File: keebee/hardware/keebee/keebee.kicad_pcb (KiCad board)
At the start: 2 copper layers, 275 x 103 mm, 153 parts, among them J1 USB_B_Micro, J2 Conn_ARM_JTAG_SWD_10, SW1 SW_SPST, SW10 SW_SPST, SW11 SW_SPST, SW12 SW_SPST, SW13 SW_SPST, SW14 SW_SPST, SW15 SW_SPST, SW16 SW_SPST, SW17 SW_SPST, SW18 SW_SPST, SW19 SW_SPST, SW2 SW_SPST, SW20 SW_SPST, SW21 SW_SPST, SW22 SW_SPST, SW23 SW_SPST, SW24 SW_SPST, SW25 SW_SPST, SW26 SW_SPST, SW27 SW_SPST, SW28 SW_SPST, SW29 SW_SPST, SW3 SW_SPST, SW30 SW_SPST, SW31 SW_SPST, SW32 SW_SPST, SW33 SW_SPST, SW34 SW_SPST, SW35 SW_SPST, SW36 SW_SPST, SW37 SW_SPST, SW38 SW_SPST, SW39 SW_SPST, SW4 SW_SPST, SW41 SW_SPST, SW42 SW_SPST, SW43 SW_SPST, SW44 SW_SPST, SW45 SW_SPST, SW46 SW_SPST, SW47 SW_SPST, SW48 SW_SPST, SW49 SW_SPST, SW5 SW_SPST, SW50 SW_SPST, SW51 SW_SPST, SW52 SW_SPST, SW53 SW_SPST, SW54 SW_SPST, SW55 SW_SPST, SW56 SW_SPST, SW57 SW_SPST, SW58 SW_SPST, SW59 SW_SPST, SW6 SW_SPST, SW60 SW_SPST, SW61 SW_SPST, SW62 SW_SPST, SW63 SW_SPST, SW64 SW_SPST, SW65 SW_SPST, SW66 SW_SPST, SW67 SW_SPST, SW68 SW_SPST, SW69 SW_SPST, SW7 SW_SPST, SW70 SW_SPST, SW8 SW_SPST, SW9 SW_SPST, U1 LM1117-3.3, U2 STM32F042K6Tx

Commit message: Finish routing all nets.
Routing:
- net +3V3: track 5.67 -> 415.1 mm, vias 0 -> 7
- net Net-(J1-Pad3): track 0.00 -> 187.2 mm, vias 0 -> 3
- net Net-(J1-Pad2): track 0.00 -> 180.5 mm, vias 0 -> 3
- net GND: track 0.00 -> 79.7 mm, vias 0 -> 15
- net Net-(R1-Pad1): track 0.00 -> 78.6 mm, vias 0 -> 7
- net /SWCLK: track 0.00 -> 56.3 mm
- net Net-(SW40-Pad2): track 0.00 -> 55.4 mm, vias 0 -> 4
- net /SWDIO: track 0.00 -> 54.5 mm, vias 0 -> 4
- net Net-(J1-Pad6): track 0.00 -> 25.0 mm, vias 0 -> 2
- net /COL8: track 98.9 -> 119.6 mm, vias 7 -> 11
- net /COL4: track 114.1 -> 134.6 mm, vias 7 -> 9
- net /COL1: track 180.2 -> 199.8 mm, vias 7 -> 9
- net /VBUS: track 0.00 -> 13.7 mm, vias 0 -> 1
- net Net-(D6-Pad2): track 0.00 -> 8.85 mm
- net Net-(D41-Pad2): track 0.00 -> 3.05 mm
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- added copper zone on B.Cu, net GND
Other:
- net class 3.3v added: clearance 0.2, trace_width 0.5, via_dia 0.8, via_drill 0.4

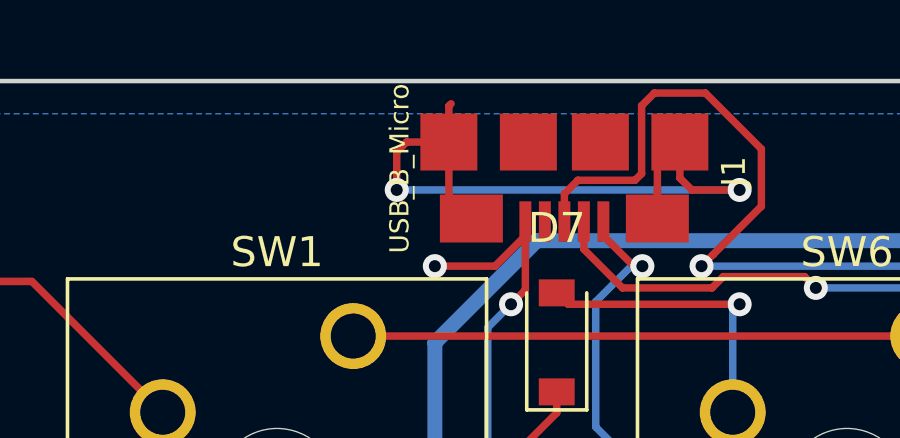
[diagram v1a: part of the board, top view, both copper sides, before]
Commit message: Minor PCB cleanup.
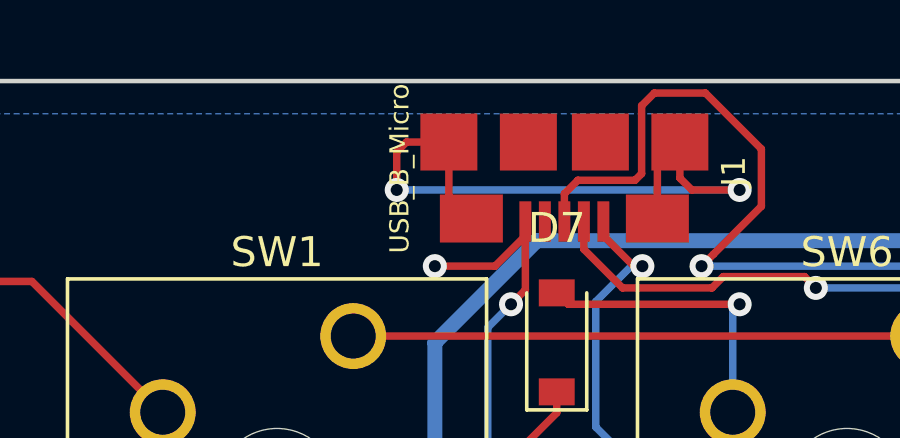
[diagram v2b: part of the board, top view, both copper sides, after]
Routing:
- net Net-(J1-Pad6): track 25.0 -> 23.7 mm
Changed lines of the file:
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@@
     (thickness 1.6)
     (drawings 936)
-    (tracks 1334)
+    (tracks 1332)
     (zones 0)
     (modules 153)
@@
   (segment (start 46.188 24.332) (end 46.938 25.082) (width 0.25) (layer F.Cu) (net 107))
   (segment (start 46.188 22.532) (end 46.188 24.332) (width 0.25) (layer F.Cu) (net 107))
-  (segment (start 46.188 21.332) (end 46.263001 21.256999) (width 0.25) (layer F.Cu) (net 107))
-  (segment (start 46.188 22.532) (end 46.188 21.332) (width 0.25) (layer F.Cu) (net 107))
   (segment (start 53.138 23.282) (end 53.888 22.532) (width 0.25) (layer F.Cu) (net 107))
   (segment (start 53.138 25.082) (end 53.138 23.282) (width 0.25) (layer F.Cu) (net 107))
